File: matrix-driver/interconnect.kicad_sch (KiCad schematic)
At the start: 6 parts, among them J2 Conn_01x08, J3 Conn_01x27, J4 Conn_01x27, J5 Conn_01x08

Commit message: added gerbers and finalized v1.0
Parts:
- removed C15, C16: 0.1uF, Capacitor_SMD:C_0402_1005Metric, symbol Device:C_Small
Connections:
- net +3.3V renamed +3V3

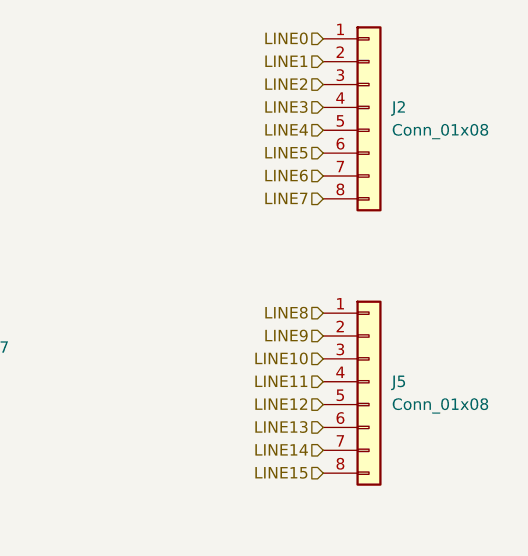
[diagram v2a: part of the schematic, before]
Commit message: changed to through hole connectors for matrix drive unit and updated schematic to reflect thermistors and reserved pin
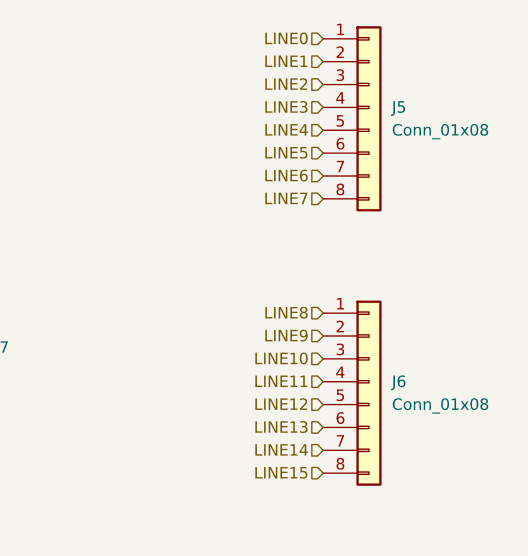
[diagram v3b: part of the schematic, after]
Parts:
- J5: renamed from J2; footprint CONN_BM08B-XASS-TF_JST:CONN_BM08B-XASS-TF_JST -> Connector_JST:JST_XA_B08B-XASK-1-A_1x08_P2.50mm_Vertical
- J6: renamed from J5; footprint CONN_BM08B-XASS-TF_JST:CONN_BM08B-XASS-TF_JST -> Connector_JST:JST_XA_B08B-XASK-1-A_1x08_P2.50mm_Vertical
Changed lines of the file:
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@@
 		(dnp no)
 		(fields_autoplaced yes)
-		(property "Reference" "J5"
+		(property "Reference" "J6"
 			(at 193.04 104.1399 0)
 			(effects
@@
 			)
 		)
-		(property "Footprint" "CONN_BM08B-XASS-TF_JST:CONN_BM08B-XASS-TF_JST"
+		(property "Footprint" "Connector_JST:JST_XA_B08B-XASK-1-A_1x08_P2.50mm_Vertical"
 			(at 190.5 104.14 0)
 			(effects
@@
 			(project "matrix-driver"
 				(path "/7405d2be-e72b-4cfa-88bf-11e2906feea4/956c8730-c940-4fda-9dee-027bcdc8455e"
-					(reference "J5")
+					(reference "J6")
 					(unit 1)
 				)
@@
 		(dnp no)
 		(fields_autoplaced yes)
-		(property "Reference" "J2"
+		(property "Reference" "J5"
 			(at 193.04 73.6599 0)
 			(effects
@@
 			)
 		)
-		(property "Footprint" "CONN_BM08B-XASS-TF_JST:CONN_BM08B-XASS-TF_JST"
+		(property "Footprint" "Connector_JST:JST_XA_B08B-XASK-1-A_1x08_P2.50mm_Vertical"
 			(at 190.5 73.66 0)
 			(effects
@@
 			(project "matrix-driver"
 				(path "/7405d2be-e72b-4cfa-88bf-11e2906feea4/956c8730-c940-4fda-9dee-027bcdc8455e"
-					(reference "J2")
-					(unit 1)
-				)
+					(reference "J5")
+					(unit 1)
+				)
